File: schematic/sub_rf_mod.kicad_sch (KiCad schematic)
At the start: 0 parts

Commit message: RF modulator completed, rough draft complete. Next step is to clean-up all pages.
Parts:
- added J4B: Conn_01x08, symbol Connector_Generic:Conn_01x08
- added RF_C10: 10pF, symbol Device:C
- added RF_C11: 270pF, symbol Device:C
- added RF_C12: 20pF, symbol Device:C
- added RF_C13: 10uF, symbol Device:C_Polarized
- added RF_C3: 10nF, symbol Device:C
- added RF_C4, RF_C5, RF_C7: 47pF, symbol Device:C
- added RF_C6, RF_C9: 82pF, symbol Device:C
- added RF_D1: 1N753, symbol Device:D_Zener
- added RF_D2: BB329A, symbol Device:D_Capacitance
- added RF_J1: RF_OUT, symbol Connector:AudioJack2
- added RF_JP1: Jumper_2_Bridged, symbol Jumper:Jumper_2_Bridged
- added RF_L1, RF_L2: 1.4uH, symbol Device:L
- added RF_L3: 1.5uH, symbol Device:L
- added RF_LV1: 8_16uH, symbol Device:L_Trim
- added RF_R1, RF_R10: 39K, symbol Device:R
- added RF_R11: 4K7, symbol Device:R
- added RF_R12: 15K, symbol Device:R
- added RF_R2, RF_R3, RF_R4: 1K, symbol Device:R
- added RF_R5, RF_R6: 270R, symbol Device:R
- added RF_R7: 47R, symbol Device:R
- added RF_R8: 82R, symbol Device:R
- added RF_R9: 8K2, symbol Device:R
- added RF_SW1: SW_SPDT, symbol Switch:SW_SPDT
- added RF_U1: LM1889, symbol RF_Modulators:LM1889
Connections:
- new net: RF_D2.1 (K), RF_LV1.1, RF_R12.2, RF_U1.15 (SOUND_TANK)
- new net: RF_JP1.1 (A), RF_LV1.2, RF_R8.2, RF_R9.2, RF_U1.14 (RF_SUPPLY), RF_U1.16 (CHROMA_SUPPLY)
- new net: RF_C12.1, RF_SW1.2 (B)
- new net: RF_C12.2, RF_C6.2, RF_L3.2, RF_R6.1, RF_U1.6 (CHB_TANK1)
- new net: RF_C11.1, RF_J1.T, RF_L1.2
- new net: RF_C10.2, RF_C9.1, RF_L1.1, RF_R7.1
- new net: RF_L2.1, RF_R8.1, RF_U1.10 (CHB_OUTPUT)
- new net: RF_C7.2, RF_R11.1, RF_R9.1, RF_U1.12 (VIDEO_IN)
- new net: RF_C10.1, RF_L2.2
- new net: RF_C3.1, RF_U1.1 (CHROMA_LEAD)
- new net: RF_C3.2, RF_C4.1, RF_R3.2
- new net: RF_C6.1, RF_L3.1, RF_R5.2, RF_SW1.1 (A), RF_U1.7 (CHB_TANK2)
- new net: RF_C5.1, RF_R2.1, RF_U1.18 (CHROMA_LAG)
- new net: RF_C7.1, RF_R12.1
- new net 2: J4B.2 (Pin_2), RF_D2.2 (A), RF_R1.2, RF_R10.2
- new net 3: J4B.3 (Pin_3), RF_U1.2 (R-Y)
- new net 5: J4B.5 (Pin_5), RF_C5.2, RF_D1.2 (A), RF_R1.1, RF_R11.2, RF_R4.2, RF_U1.3 (CHROMA_BIAS)
- new net 6: J4B.6 (Pin_6), RF_U1.13 (CHROMA_SUBCAR)
- new net 7: J4B.7 (Pin_7), RF_U1.4 (B-Y)
- new net 8: J4B.8 (Pin_8), RF_C4.2, RF_R2.2
- new net GNDD: J4B.1 (Pin_1), RF_C11.2, RF_C13.2, RF_C9.2, RF_J1.S, RF_R3.1, RF_R4.1, RF_R7.2, RF_U1.5 (GND)
- new net VDDF: J4B.4 (Pin_4), RF_C13.1, RF_D1.1 (K), RF_JP1.2 (B), RF_R10.1, RF_R5.1, RF_R6.2
- no-connect marks 0 -> 4

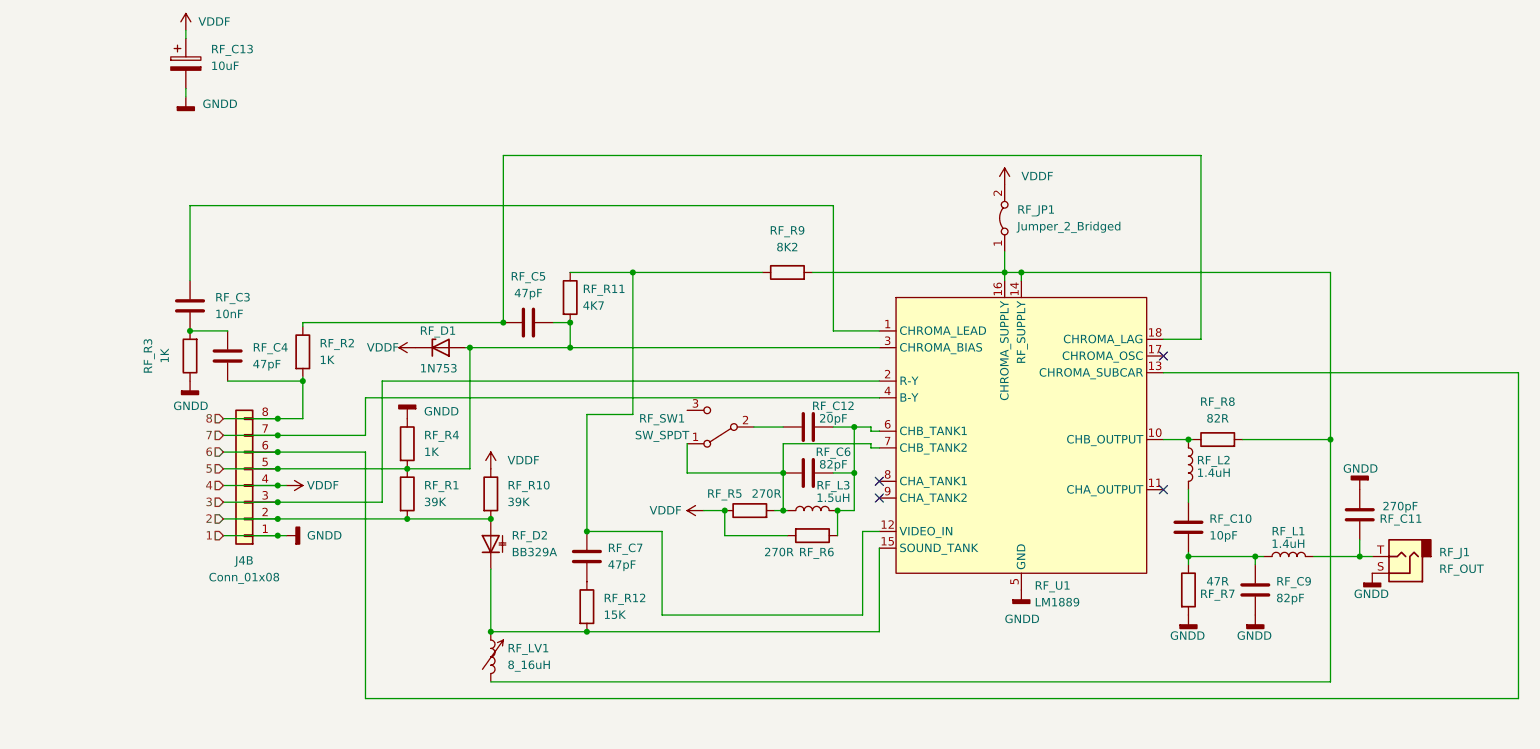
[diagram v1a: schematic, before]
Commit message: cleaup of rf circuits. much better flow vs the original. Comparing to the wiki.console5.com/wiki/Colecovision shows many differences. Not sure I agree with it at all. Going to use the ADAM schematic instead since even the dual adjustable coils is not a thing in my circuit. Revision difference?
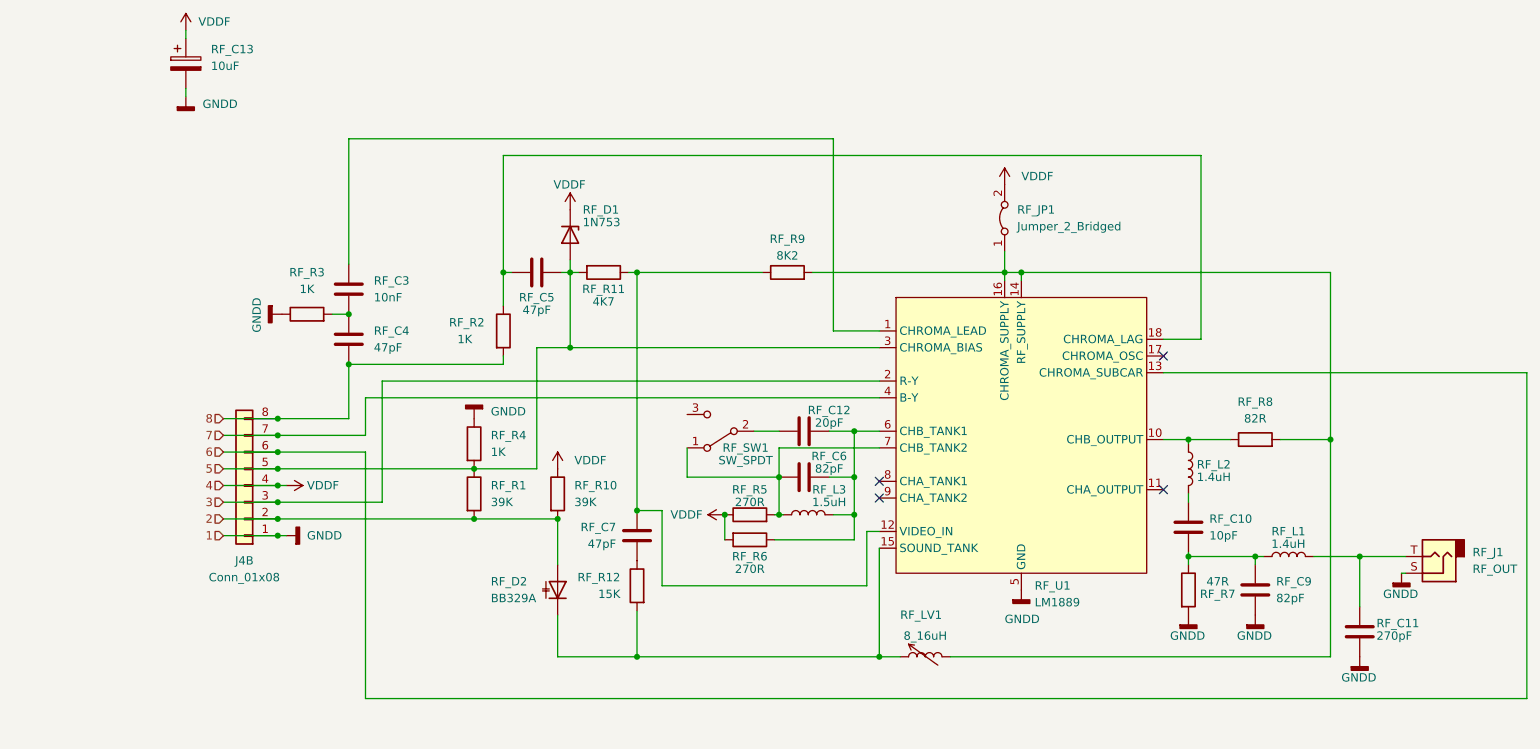
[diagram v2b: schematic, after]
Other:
- moved on the sheet: RF_C11, RF_C12, RF_C3, RF_C4, RF_C5, RF_C6, RF_C7, RF_D1, RF_D2, RF_J1, RF_L2, RF_L3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

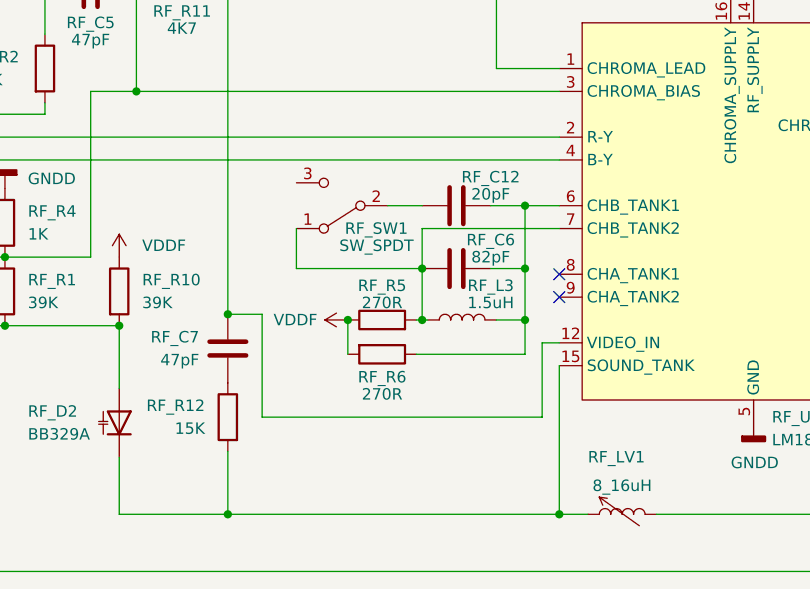
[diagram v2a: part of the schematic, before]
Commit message: cleaned up RF circuit again, and used ChildOfCv schematic as a ref. Fixed a few mistakes. I didn't know his even existed. Its a very nice project. I didn't know it existed till I was googling some sources for the RF part, since the ADAM was different. Though his RF circuit for the daughter board is different in ways that don't make sense for mine. I'll have to double check that by hand.
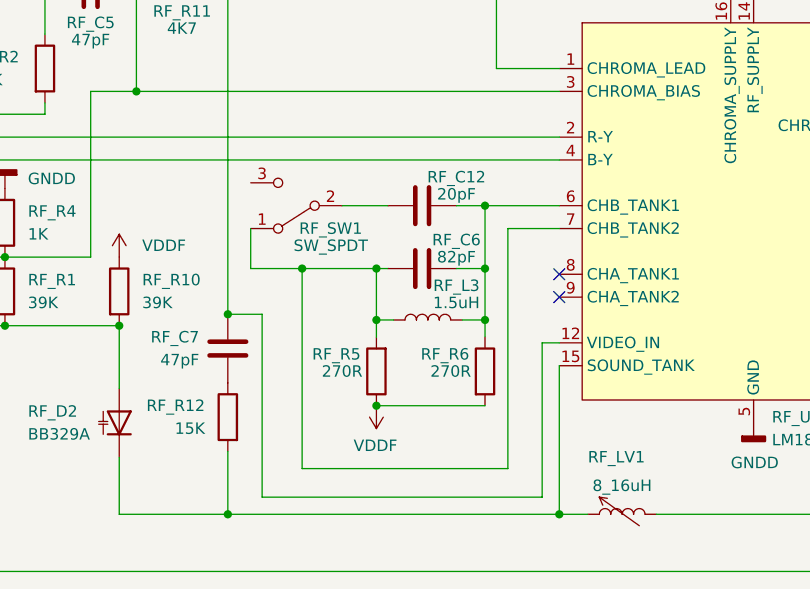
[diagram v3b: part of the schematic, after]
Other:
- moved on the sheet: RF_C12, RF_C6, RF_L3, RF_R5, RF_R6, RF_SW1

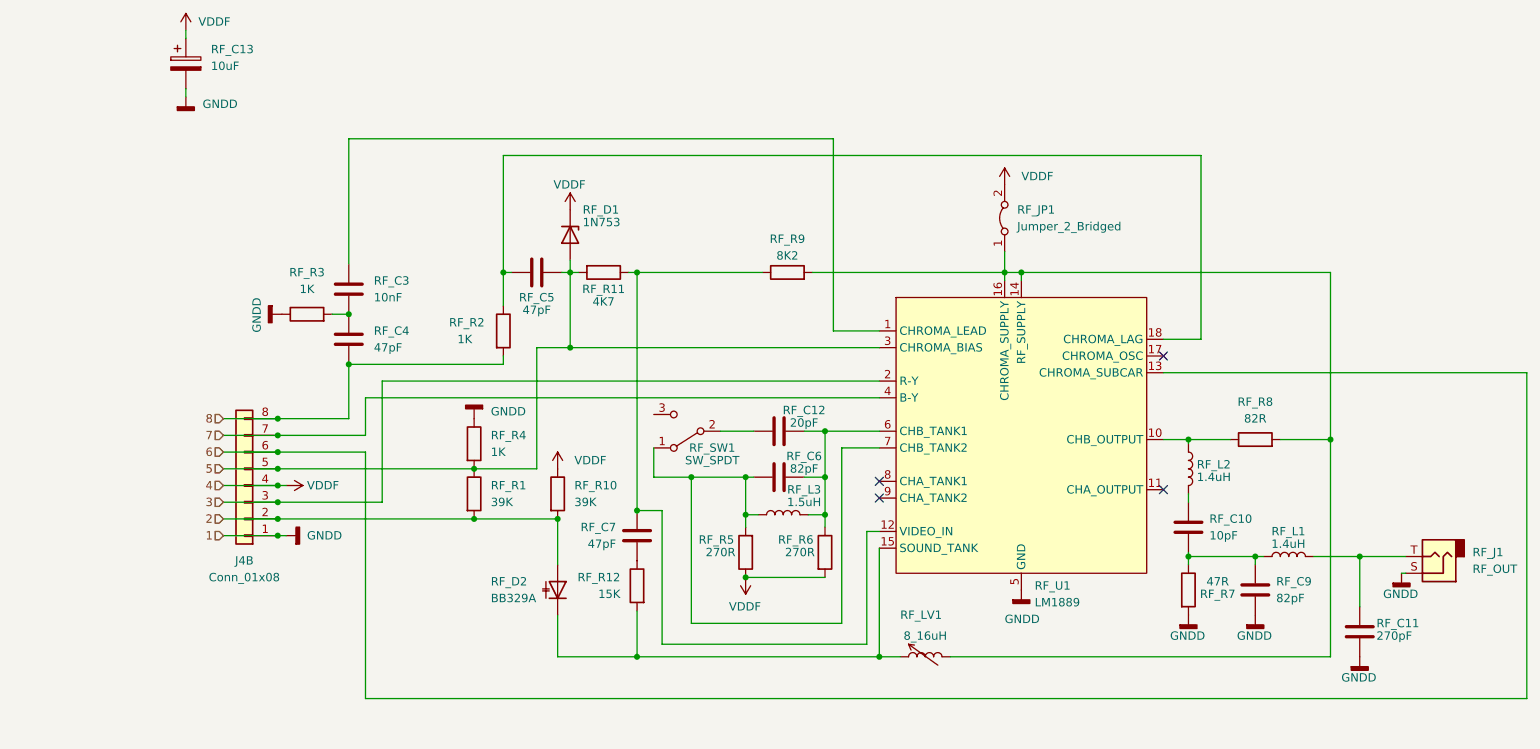
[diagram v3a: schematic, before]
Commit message: all lines renamed, based most of the names from the coleco adam schematic. CS cart lines are my own, and the rest are from the wiki schematic for the controller... those will need to be checked.
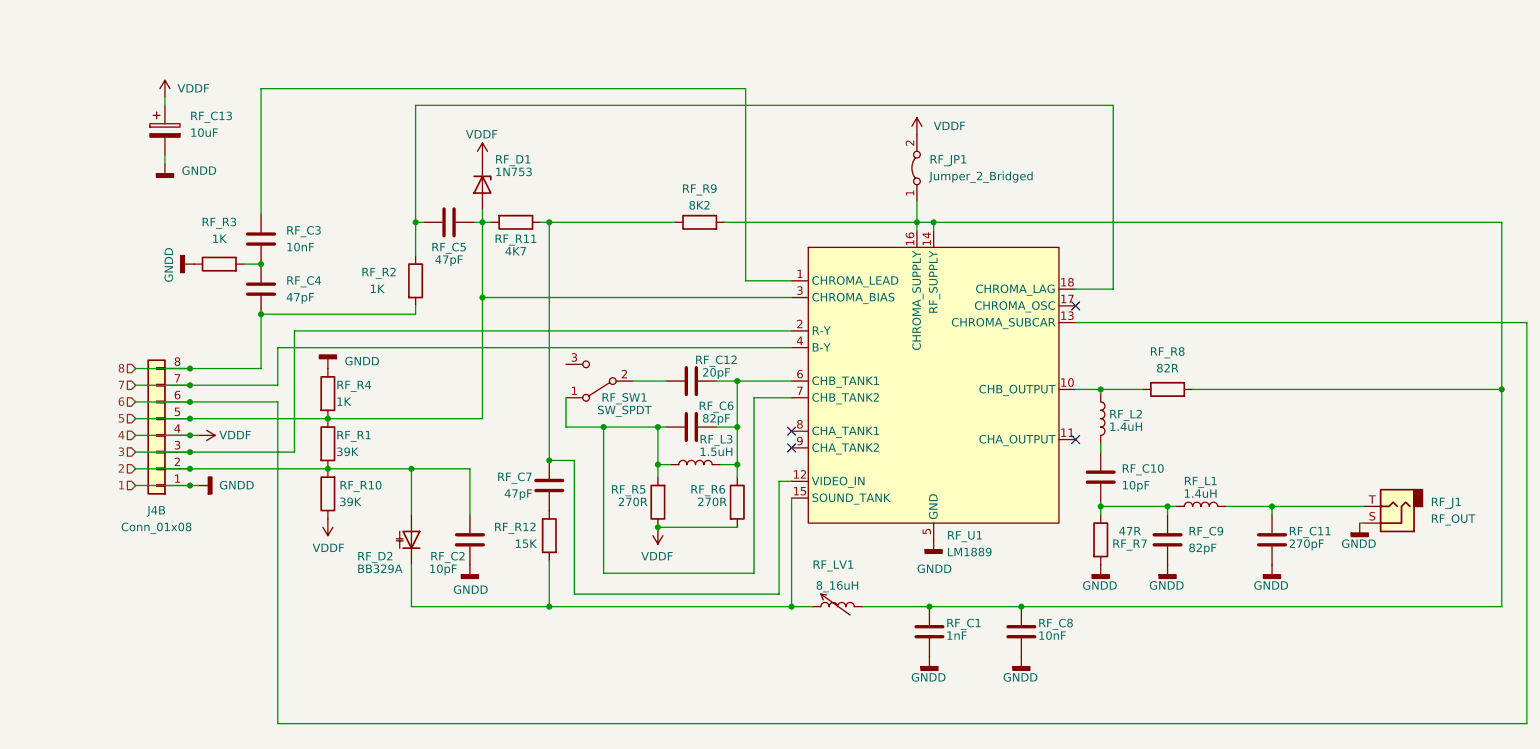
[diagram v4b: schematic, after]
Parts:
- added RF_C1: 1nF, symbol Device:C
- added RF_C2: 10pF, symbol Device:C
- added RF_C8: 10nF, symbol Device:C
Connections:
- net 2: now also RF_C2.2
- net GNDD: now also RF_C1.2, RF_C2.1, RF_C8.2
- net at RF_JP1.1 (A), RF_LV1.2, RF_R8.2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: now also RF_C1.1, RF_C8.1
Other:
- moved on the sheet: J4B, RF_C10, RF_C11, RF_C12, RF_C13, RF_C3, RF_C4, RF_C5, RF_C6, RF_C7, RF_C9, RF_D1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

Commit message: adjusted size of the sheets. added pcb version to the rev field. F.0... the 0 is for future fixes on my end. RF PCB is E.0.
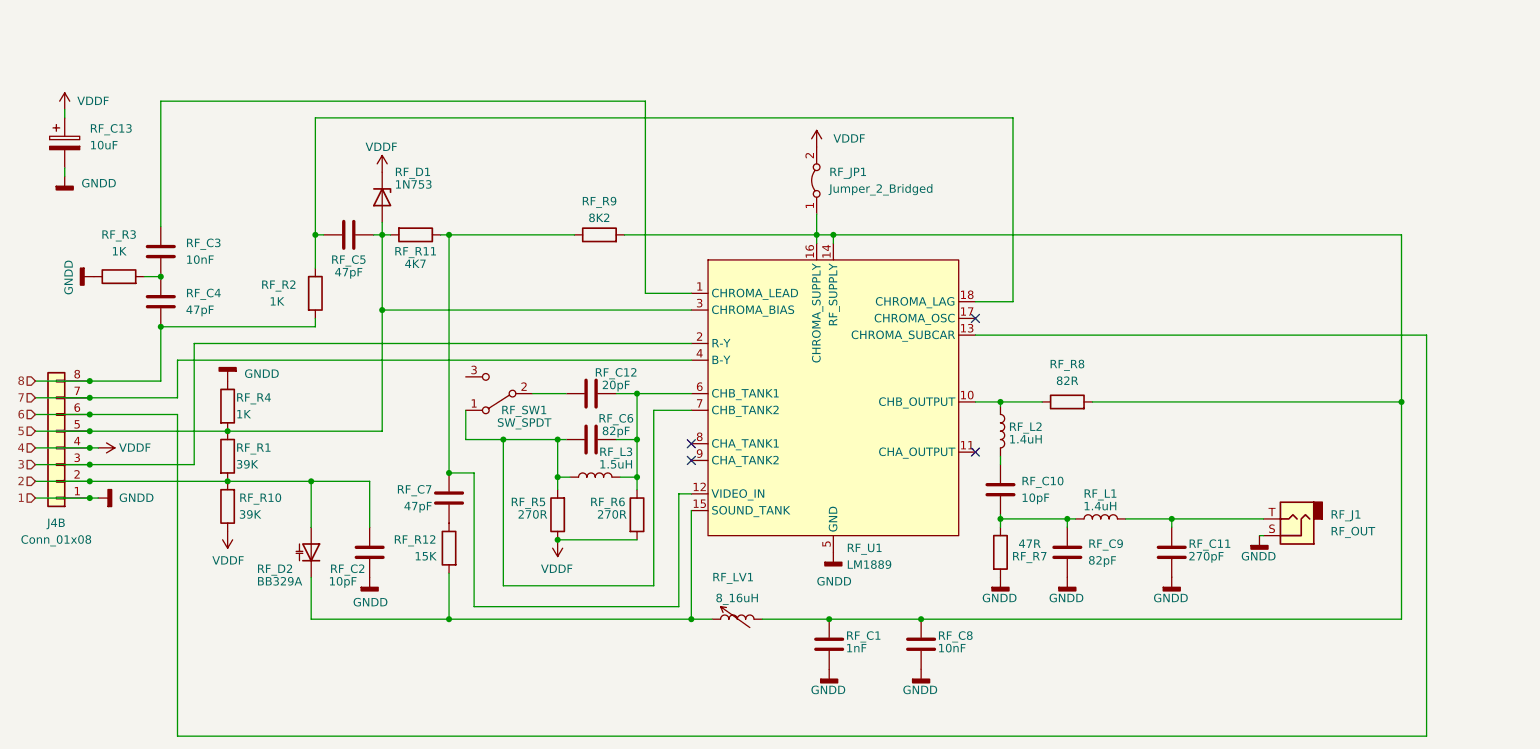
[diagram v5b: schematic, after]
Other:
- title: (none) -> Colecovision Schematic
- moved on the sheet: J4B, RF_C1, RF_C10, RF_C11, RF_C12, RF_C13, RF_C2, RF_C3, RF_C4, RF_C5, RF_C6, RF_C7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

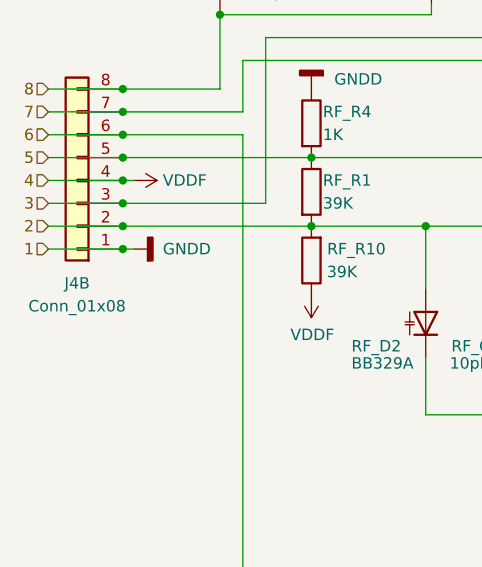
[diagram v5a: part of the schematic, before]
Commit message: cleanup, and started associating components
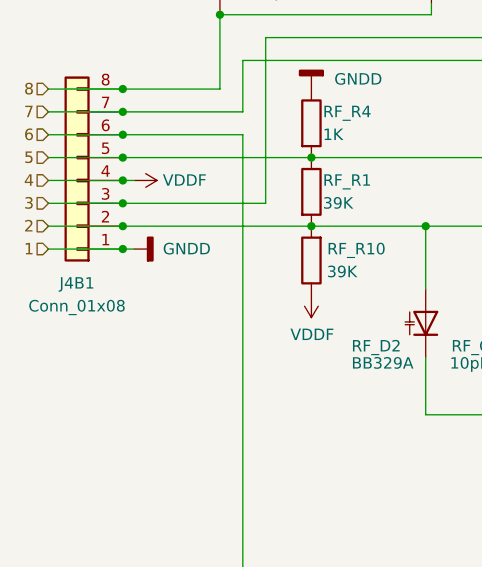
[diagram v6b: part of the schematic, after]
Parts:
- J4B1: renamed from J4B; footprint (none) -> Connector_PinHeader_2.54mm:PinHeader_1x08_P2.54mm_Vertical
- RF_C1, RF_C10, RF_C11, RF_C12, RF_C2, RF_C3, RF_C4, RF_C5, RF_C6, RF_C7, RF_C8, RF_C9: footprint (none) -> Capacitor_THT:C_Disc_D7.0mm_W2.5mm_P5.00mm
- RF_C13: footprint (none) -> Capacitor_THT:CP_Radial_D5.0mm_P2.00mm
- RF_D1, RF_D2: footprint (none) -> Diode_THT:D_DO-35_SOD27_P10.16mm_Horizontal
- RF_JP1: footprint (none) -> Resistor_THT:R_Bare_Metal_Element_L16.3mm_W4.8mm_P15.30mm
- RF_L1, RF_L2, RF_L3: footprint (none) -> Inductor_THT:L_Radial_D7.5mm_P5.00mm_Fastron_07P
- RF_R1, RF_R10, RF_R11, RF_R12, RF_R2, RF_R3, RF_R4, RF_R5, RF_R6, RF_R7, RF_R8, RF_R9: footprint (none) -> Resistor_THT:R_Axial_DIN0207_L6.3mm_D2.5mm_P7.62mm_Horizontal
- RF_SW1: footprint (none) -> Button_Switch_THT:SW_CuK_OS102011MA1QN1_SPDT_Angled
- RF_U1: footprint (none) -> Package_DIP:DIP-18_W7.62mm_LongPads
